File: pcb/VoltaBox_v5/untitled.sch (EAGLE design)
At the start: 58 parts, among them J1 1050170001, X1 112J-TDAR-R(MICROSD), X2 52892-0895, X3 52892-0895, X4 292304-3

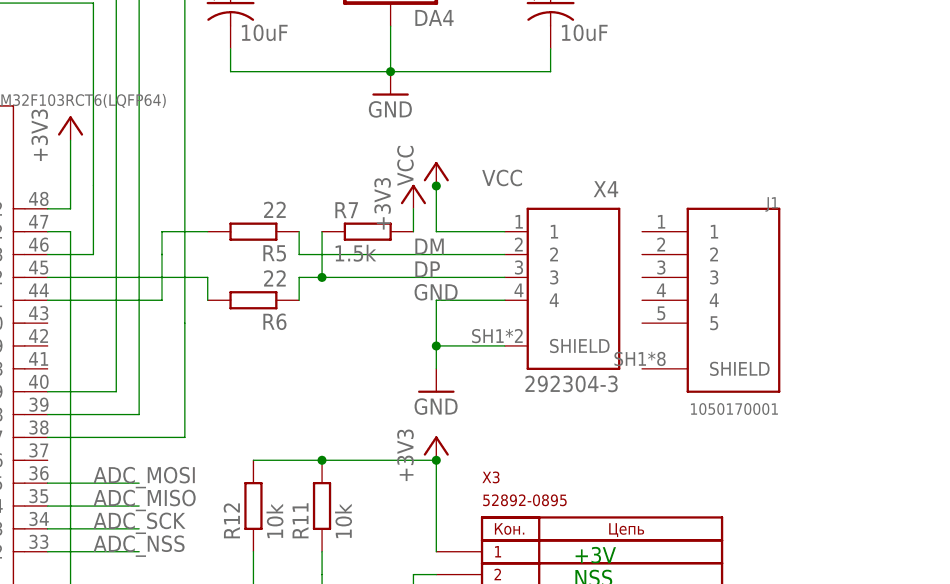
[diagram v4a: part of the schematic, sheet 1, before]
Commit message: usb route done, some pcb and schematic changes, added power connectors, dc-dc diode replaced, added TODO file
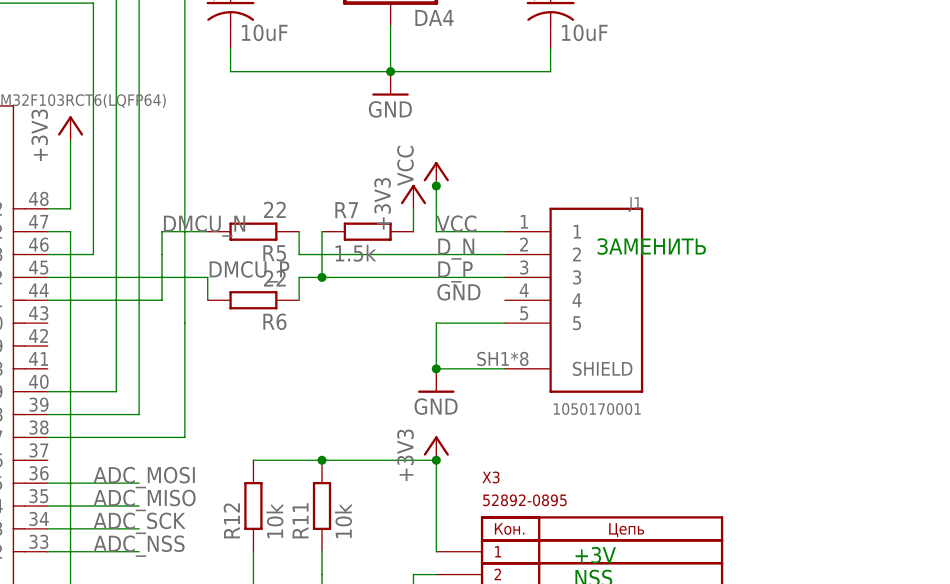
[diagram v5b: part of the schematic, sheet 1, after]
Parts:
- added X6: XT60PW-M, untitled:XT60PW-M
- D1: value STPS3L60U -> STPS5L60S; device untitled:STPS3L60U -> untitled:STPS5L60S
- X4: value 292304-3 -> XT30PW-F; device 292304-3:292304-3 -> untitled:XT30PW-F
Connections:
- net N$20 renamed DMCU_P
- net N$21 renamed DMCU_N
- removed net DM: R5.1, X4.2
- removed net DP: R6.1, R7.1, X4.3
- new net D_N: J1.2, R5.1
- new net D_P: J1.3, R6.1, R7.1
- net +12V: now also X6.P$1
- net +4V: now also X4.P$1
- net GND: now also J1.5, J1.SHIELD, X6.P$2; no longer X4.4, X4.SHIELD
- net N$23: now also X4.P$2
- net VCC: now also J1.1; no longer X4.1
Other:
- note added: "ЗАМЕНИТЬ"
- moved on the sheet: J1
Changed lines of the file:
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@@
 <class number="0" name="default" width="0" drill="0">
+</class>
+<class number="1" name="diff pair" width="0.700025" drill="0">
+<clearance class="1" value="0.2"/>
 </class>
 </classes>
@@
 <part name="+3V9" library="supply1" library_urn="urn:adsk.eagle:library:371" deviceset="+3V3" device=""/>
 <part name="P+4" library="supply1" library_urn="urn:adsk.eagle:library:371" deviceset="VCC" device=""/>
-<part name="D1" library="untitled" deviceset="STPS3L60U" device=""/>
 <part name="C18" library="eagle-ltspice" library_urn="urn:adsk.eagle:library:217" deviceset="C" device="C0603" package3d_urn="urn:adsk.eagle:package:13262/1" value="0.1u"/>
 <part name="C19" library="eagle-ltspice" library_urn="urn:adsk.eagle:library:217" deviceset="C" device="C0603" package3d_urn="urn:adsk.eagle:package:13262/1" value="0.1u"/>
@@
 <part name="C31" library="eagle-ltspice" library_urn="urn:adsk.eagle:library:217" deviceset="C" device="C0603" package3d_urn="urn:adsk.eagle:package:13262/1" value="0.1u"/>
 <part name="GND19" library="supply1" library_urn="urn:adsk.eagle:library:371" deviceset="GND" device=""/>
-<part name="X4" library="292304-3" deviceset="292304-3" device=""/>
 <part name="X2" library="52892-0895" deviceset="52892-0895" device=""/>
 <part name="X3" library="52892-0895" deviceset="52892-0895" device=""/>
@@
 <part name="J1" library="1050170001" deviceset="1050170001" device=""/>
 <part name="C21" library="rcl" library_urn="urn:adsk.eagle:library:334" deviceset="CPOL-US" device="150CLZ-1014" package3d_urn="urn:adsk.eagle:package:23405/1" value="100u"/>
+<part name="D1" library="untitled" deviceset="STPS5L60S" device=""/>
+<part name="X6" library="untitled" deviceset="XT60PW-M" device=""/>
+<part name="P+6" library="supply1" library_urn="urn:adsk.eagle:library:371" deviceset="+12V" device=""/>
+<part name="X4" library="untitled" deviceset="XT30PW-F" device=""/>
+<part name="U$6" library="untitled" deviceset="+4V" device=""/>
 </parts>
 <sheets>
@@
 <text x="152.4" y="29.21" size="1.778" layer="91">GND</text>
 <text x="152.4" y="46.99" size="1.778" layer="91">+3V</text>
+<text x="154.94" y="81.28" size="1.778" layer="91">ЗАМЕНИТЬ</text>
 </plain>
 <instances>
@@
 <instance part="ZQ2" gate="G$1" x="5.08" y="68.58"/>
 <instance part="ZQ1" gate="G$1" x="-17.78" y="68.58"/>
-<instance part="X4" gate="G$1" x="152.4" y="77.47" rot="MR0"/>
 <instance part="X2" gate="G$1" x="-2.54" y="137.16" rot="MR0"/>
 <instance part="X3" gate="G$1" x="157.48" y="40.64"/>
@@
 <instance part="C9" gate="G$1" x="190.5" y="149.86"/>
 <instance part="GND14" gate="1" x="33.02" y="124.46"/>
-<instance part="J1" gate="G$1" x="170.18" y="76.2" rot="MR0"/>
+<instance part="J1" gate="G$1" x="154.94" y="76.2" rot="MR0"/>
 </instances>
 <busses>
@@
 </segment>
 <segment>
-<wire x1="144.78" y1="76.2" x2="137.16" y2="76.2" width="0.1524" layer="91"/>
-<wire x1="137.16" y1="76.2" x2="137.16" y2="71.12" width="0.1524" layer="91"/>
-<wire x1="137.16" y1="71.12" x2="144.78" y2="71.12" width="0.1524" layer="91"/>
+<wire x1="144.78" y1="73.66" x2="137.16" y2="73.66" width="0.1524" layer="91"/>
+<wire x1="137.16" y1="73.66" x2="137.16" y2="68.58" width="0.1524" layer="91"/>
+<wire x1="137.16" y1="68.58" x2="144.78" y2="68.58" width="0.1524" layer="91"/>
 <pinref part="GND16" gate="1" pin="GND"/>
-<wire x1="137.16" y1="68.58" x2="137.16" y2="71.12" width="0.1524" layer="91"/>
-<junction x="137.16" y="71.12"/>
-<label x="134.62" y="76.2" size="1.778" layer="95"/>
-<pinref part="X4" gate="G$1" pin="4"/>
-<pinref part="X4" gate="G$1" pin="SHIELD"/>
+<junction x="137.16" y="68.58"/>
+<label x="137.16" y="76.2" size="1.778" layer="95"/>
+<pinref part="J1" gate="G$1" pin="5"/>
+<pinref part="J1" gate="G$1" pin="SHIELD"/>
 </segment>
 <segment>
@@
 <wire x1="137.16" y1="88.9" x2="137.16" y2="83.82" width="0.1524" layer="91"/>
 <junction x="137.16" y="88.9"/>
-<label x="142.24" y="88.9" size="1.778" layer="95"/>
-<pinref part="X4" gate="G$1" pin="1"/>
+<label x="137.16" y="83.82" size="1.778" layer="95"/>
+<pinref part="J1" gate="G$1" pin="1"/>
 </segment>
 </net>
@@
 </segment>
 </net>
-<net name="DM" class="0">
+<net name="D_N" class="1">
 <segment>
 <pinref part="R5" gate="G$1" pin="1"/>
 <wire x1="121.92" y1="83.82" x2="121.92" y2="81.28" width="0.1524" layer="91"/>
 <wire x1="121.92" y1="81.28" x2="144.78" y2="81.28" width="0.1524" layer="91"/>
-<label x="134.62" y="81.28" size="1.778" layer="95"/>
-<pinref part="X4" gate="G$1" pin="2"/>
-</segment>
-</net>
-<net name="DP" class="0">
+<label x="137.16" y="81.28" size="1.778" layer="95"/>
+<pinref part="J1" gate="G$1" pin="2"/>
+</segment>
+</net>
+<net name="D_P" class="1">
 <segment>
 <pinref part="R6" gate="G$1" pin="1"/>
@@
 <wire x1="124.46" y1="83.82" x2="124.46" y2="78.74" width="0.1524" layer="91"/>
 <junction x="124.46" y="78.74"/>
-<label x="134.62" y="78.74" size="1.778" layer="95"/>
-<pinref part="X4" gate="G$1" pin="3"/>
-</segment>
-</net>
-<net name="N$20" class="0">
+<label x="137.16" y="78.74" size="1.778" layer="95"/>
+<pinref part="J1" gate="G$1" pin="3"/>
+</segment>
+</net>
+<net name="DMCU_P" class="1">
 <segment>
 <pinref part="DD1" gate="G$1" pin="PA12"/>
@@
 <pinref part="R6" gate="G$1" pin="2"/>
 <wire x1="111.76" y1="78.74" x2="111.76" y2="76.2" width="0.1524" layer="91"/>
-</segment>
-</net>
-<net name="N$21" class="0">
+<label x="111.76" y="78.74" size="1.778" layer="95"/>
+</segment>
+</net>
+<net name="DMCU_N" class="1">
 <segment>
 <pinref part="R5" gate="G$1" pin="2"/>
@@
 <pinref part="DD1" gate="G$1" pin="PA11"/>
 <wire x1="106.68" y1="76.2" x2="93.98" y2="76.2" width="0.1524" layer="91"/>
+<label x="106.68" y="83.82" size="1.778" layer="95"/>
 </segment>
 </net>
@@
 <instances>
 <instance part="P+4" gate="VCC" x="7.62" y="2.54"/>
-<instance part="D1" gate="G$1" x="50.8" y="25.4" rot="R90"/>
 <instance part="C18" gate="G$1" x="25.4" y="38.1" rot="R90"/>
 <instance part="C19" gate="G$1" x="76.2" y="25.4"/>
@@
 <instance part="U$8" gate="G$1" x="7.62" y="12.7"/>
 <instance part="U$9" gate="G$1" x="43.18" y="12.7"/>
-<instance part="U$10" gate="G$1" x="15.24" y="5.08"/>
+<instance part="U$10" gate="G$1" x="-15.24" y="-12.7"/>
 <instance part="R4" gate="G$1" x="86.36" y="22.86" rot="R90"/>
 <instance part="R8" gate="1" x="101.6" y="25.4" rot="R180"/>
@@
 <instance part="C23" gate="G$1" x="-2.54" y="43.18"/>
 <instance part="C21" gate="G$1" x="68.58" y="25.4"/>
+<instance part="D1" gate="G$1" x="50.8" y="25.4" rot="R90"/>
+<instance part="X6" gate="G$1" x="-15.24" y="-7.62"/>
+<instance part="P+6" gate="1" x="-15.24" y="-5.08"/>
+<instance part="X4" gate="G$1" x="142.24" y="22.86"/>
+<instance part="U$6" gate="G$1" x="142.24" y="25.4"/>
 </instances>
 <busses>
@@
 </segment>
 <segment>
-<pinref part="D1" gate="G$1" pin="A"/>
 <pinref part="U$3" gate="G$1" pin="GND"/>
 <wire x1="50.8" y1="22.86" x2="50.8" y2="15.24" width="0.1524" layer="91"/>
+<pinref part="D1" gate="G$1" pin="A"/>
 </segment>
 <segment>
@@
 <pinref part="C23" gate="G$1" pin="2"/>
 </segment>
+<segment>
+<pinref part="X6" gate="G$1" pin="P$2"/>
+<pinref part="U$10" gate="G$1" pin="GND"/>
+</segment>
 </net>
 <net name="N$4" class="0">
@@
 <wire x1="38.1" y1="38.1" x2="38.1" y2="30.48" width="0.1524" layer="91"/>
 <wire x1="38.1" y1="30.48" x2="50.8" y2="30.48" width="0.1524" layer="91"/>
-<pinref part="D1" gate="G$1" pin="C"/>
-<wire x1="50.8" y1="30.48" x2="50.8" y2="27.94" width="0.1524" layer="91"/>
 <pinref part="DA1" gate="G$1" pin="SW"/>
 <junction x="38.1" y="30.48"/>
 <pinref part="L1" gate="G$1" pin="1"/>
+<pinref part="D1" gate="G$1" pin="C"/>
+<wire x1="50.8" y1="30.48" x2="50.8" y2="27.94" width="0.1524" layer="91"/>
 <junction x="50.8" y="30.48"/>
 </segment>
@@
 <pinref part="C25" gate="G$1" pin="1"/>
 <junction x="22.86" y="-22.86"/>
+</segment>
+<segment>
+<pinref part="P+6" gate="1" pin="+12V"/>
+<pinref part="X6" gate="G$1" pin="P$1"/>
 </segment>
 </net>
@@
 <pinref part="C21" gate="G$1" pin="+"/>
 </segment>
+<segment>
+<pinref part="U$6" gate="G$1" pin="+4V"/>
+<pinref part="X4" gate="G$1" pin="P$1"/>
+</segment>
 </net>
 <net name="+5V" class="0">
@@
 <wire x1="132.08" y1="-7.62" x2="132.08" y2="10.16" width="0.1524" layer="91"/>
 <wire x1="132.08" y1="10.16" x2="142.24" y2="10.16" width="0.1524" layer="91"/>
-<wire x1="142.24" y1="10.16" x2="142.24" y2="7.62" width="0.1524" layer="91"/>
+<wire x1="142.24" y1="10.16" x2="142.24" y2="20.32" width="0.1524" layer="91"/>
 <junction x="132.08" y="10.16"/>
-</segment>
-</net>
+<pinref part="X4" gate="G$1" pin="P$2"/>
+</segment>
+</net>

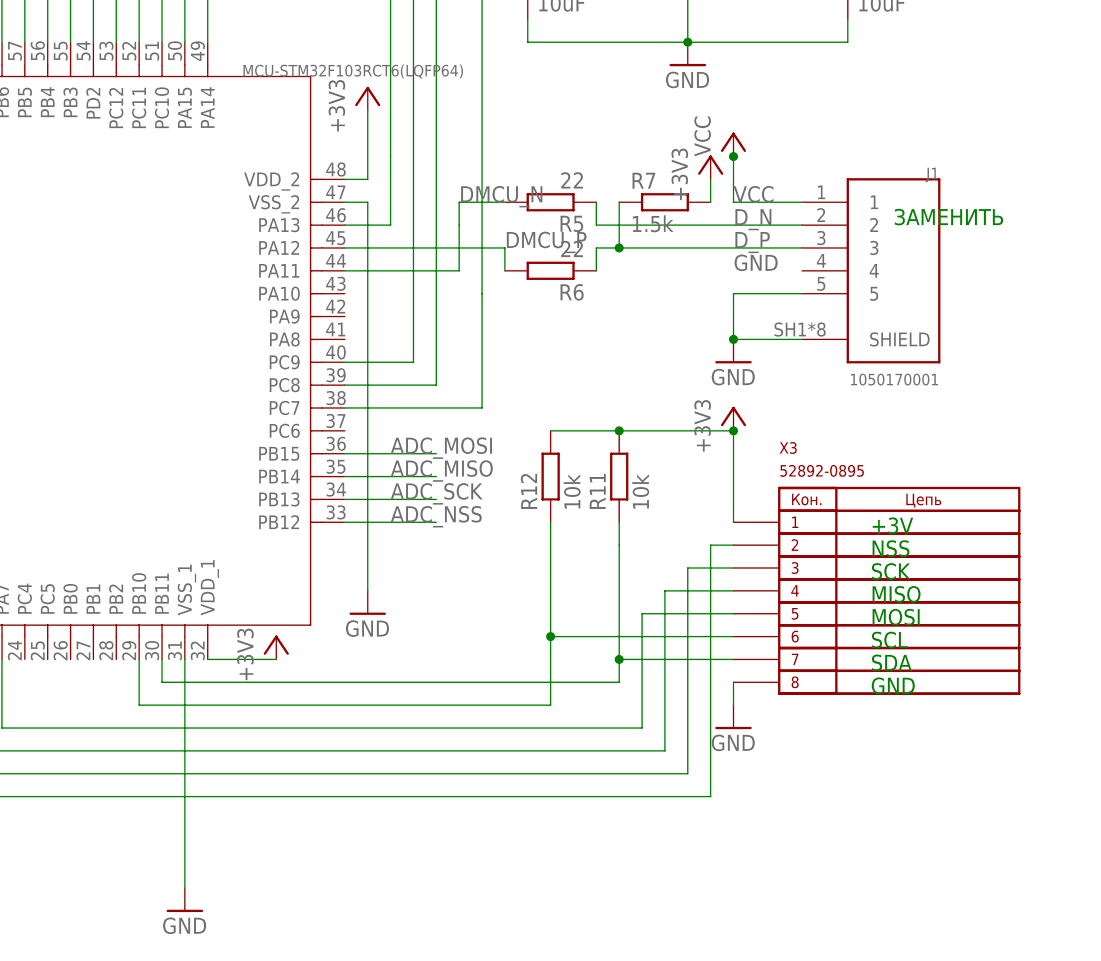
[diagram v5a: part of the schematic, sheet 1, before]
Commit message: pcb adaptation for existing case
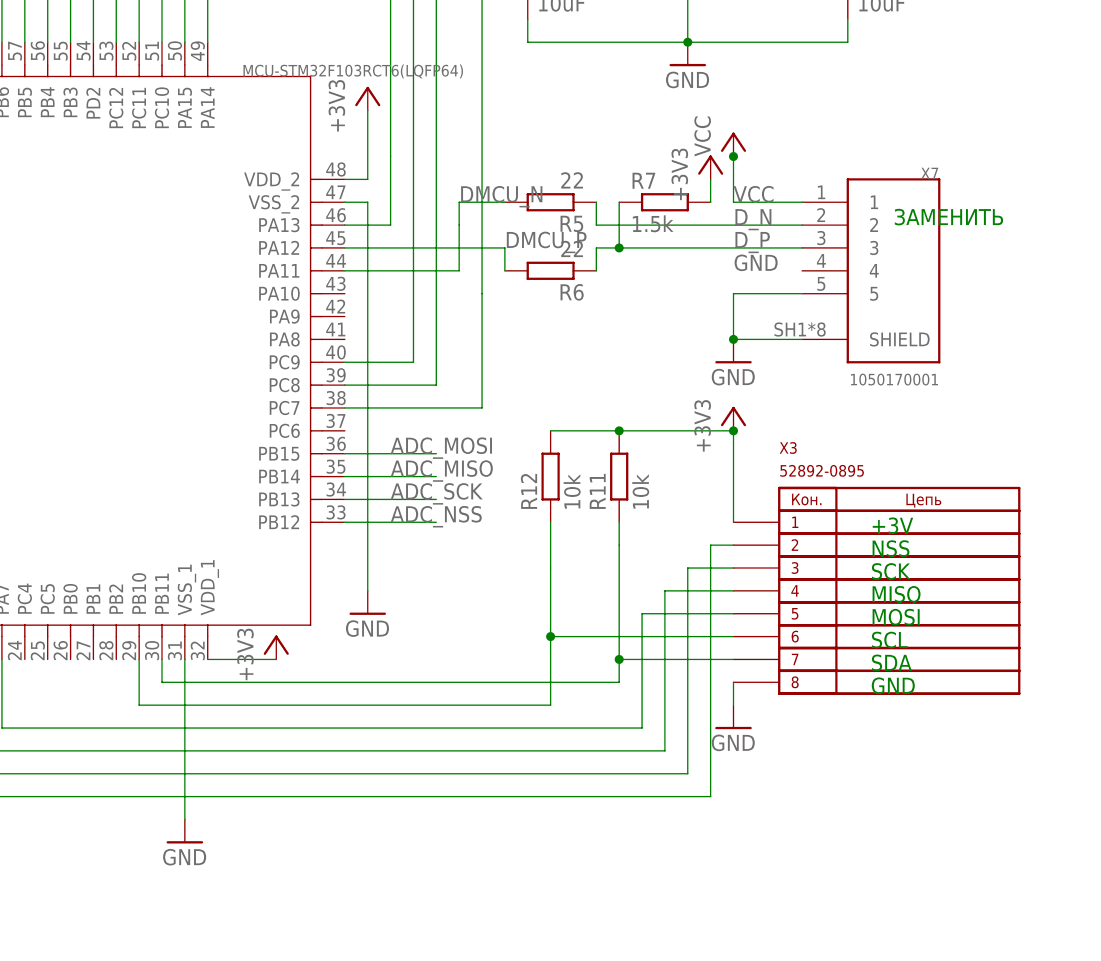
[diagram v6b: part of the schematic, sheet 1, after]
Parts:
- renumbered J1 to X7
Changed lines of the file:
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@@
 <part name="GND2" library="supply1" library_urn="urn:adsk.eagle:library:371" deviceset="GND" device=""/>
 <part name="GND3" library="supply1" library_urn="urn:adsk.eagle:library:371" deviceset="GND" device=""/>
-<part name="GND4" library="supply1" library_urn="urn:adsk.eagle:library:371" deviceset="GND" device=""/>
+<part name="GND" library="supply1" library_urn="urn:adsk.eagle:library:371" deviceset="GND" device=""/>
 <part name="GND5" library="supply1" library_urn="urn:adsk.eagle:library:371" deviceset="GND" device=""/>
 <part name="GND6" library="supply1" library_urn="urn:adsk.eagle:library:371" deviceset="GND" device=""/>
@@
 <part name="C23" library="rcl" library_urn="urn:adsk.eagle:library:334" deviceset="C-EU" device="C2220K" package3d_urn="urn:adsk.eagle:package:23687/2" value="4.7u"/>
 <part name="GND14" library="supply1" library_urn="urn:adsk.eagle:library:371" deviceset="GND" device=""/>
-<part name="J1" library="1050170001" deviceset="1050170001" device=""/>
+<part name="X7" library="1050170001" deviceset="1050170001" device=""/>
 <part name="C21" library="rcl" library_urn="urn:adsk.eagle:library:334" deviceset="CPOL-US" device="150CLZ-1014" package3d_urn="urn:adsk.eagle:package:23405/1" value="100u"/>
 <part name="D1" library="untitled" deviceset="STPS5L60S" device=""/>
@@
 <instance part="GND2" gate="1" x="10.16" y="55.88"/>
 <instance part="GND3" gate="1" x="43.18" y="25.4"/>
-<instance part="GND4" gate="1" x="76.2" y="5.08"/>
+<instance part="GND" gate="1" x="76.2" y="12.7"/>
 <instance part="GND5" gate="1" x="-15.24" y="91.44"/>
 <instance part="GND6" gate="1" x="129.54" y="142.24"/>
@@
 <instance part="C9" gate="G$1" x="190.5" y="149.86"/>
 <instance part="GND14" gate="1" x="33.02" y="124.46"/>
-<instance part="J1" gate="G$1" x="154.94" y="76.2" rot="MR0"/>
+<instance part="X7" gate="G$1" x="154.94" y="76.2" rot="MR0"/>
 </instances>
 <busses>
@@
 <segment>
 <pinref part="DD1" gate="G$1" pin="VSS_1"/>
-<pinref part="GND4" gate="1" pin="GND"/>
-<wire x1="76.2" y1="7.62" x2="76.2" y2="33.02" width="0.1524" layer="91"/>
+<pinref part="GND" gate="1" pin="GND"/>
+<wire x1="76.2" y1="15.24" x2="76.2" y2="33.02" width="0.1524" layer="91"/>
 </segment>
 <segment>
@@
 <junction x="137.16" y="68.58"/>
 <label x="137.16" y="76.2" size="1.778" layer="95"/>
-<pinref part="J1" gate="G$1" pin="5"/>
-<pinref part="J1" gate="G$1" pin="SHIELD"/>
+<pinref part="X7" gate="G$1" pin="5"/>
+<pinref part="X7" gate="G$1" pin="SHIELD"/>
 </segment>
 <segment>
@@
 <junction x="137.16" y="88.9"/>
 <label x="137.16" y="83.82" size="1.778" layer="95"/>
-<pinref part="J1" gate="G$1" pin="1"/>
+<pinref part="X7" gate="G$1" pin="1"/>
 </segment>
 </net>
@@
 <wire x1="121.92" y1="81.28" x2="144.78" y2="81.28" width="0.1524" layer="91"/>
 <label x="137.16" y="81.28" size="1.778" layer="95"/>
-<pinref part="J1" gate="G$1" pin="2"/>
+<pinref part="X7" gate="G$1" pin="2"/>
 </segment>
 </net>
@@
 <junction x="124.46" y="78.74"/>
 <label x="137.16" y="78.74" size="1.778" layer="95"/>
-<pinref part="J1" gate="G$1" pin="3"/>
+<pinref part="X7" gate="G$1" pin="3"/>
 </segment>
 </net>
@@
 <pinref part="DA3" gate="G$1" pin="SDO"/>
 <wire x1="167.64" y1="-15.24" x2="177.8" y2="-15.24" width="0.1524" layer="91"/>
-<wire x1="177.8" y1="-15.24" x2="177.8" y2="-86.36" width="0.1524" layer="91"/>
-<wire x1="177.8" y1="-86.36" x2="53.34" y2="-86.36" width="0.1524" layer="91"/>
-<wire x1="53.34" y1="-86.36" x2="53.34" y2="-38.1" width="0.1524" layer="91"/>
+<wire x1="177.8" y1="-15.24" x2="177.8" y2="-76.2" width="0.1524" layer="91"/>
+<wire x1="177.8" y1="-76.2" x2="53.34" y2="-76.2" width="0.1524" layer="91"/>
+<wire x1="53.34" y1="-76.2" x2="53.34" y2="-38.1" width="0.1524" layer="91"/>
 <pinref part="DD2" gate="A" pin="VID"/>
 <wire x1="53.34" y1="-38.1" x2="76.2" y2="-38.1" width="0.1524" layer="91"/>
